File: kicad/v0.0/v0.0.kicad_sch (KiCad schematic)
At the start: 49 parts, among them J1 USB_B_Micro, J2 9V_IN, J3 LED, J4 MOTOR, Q1 IRF520, SW1 SW_Push, SW2 SW_Push, U1 MCP2221AxSL, U2 MAX14872ETC+, U3 ESP32-WROOM-32, U6 AZ1117-3.3

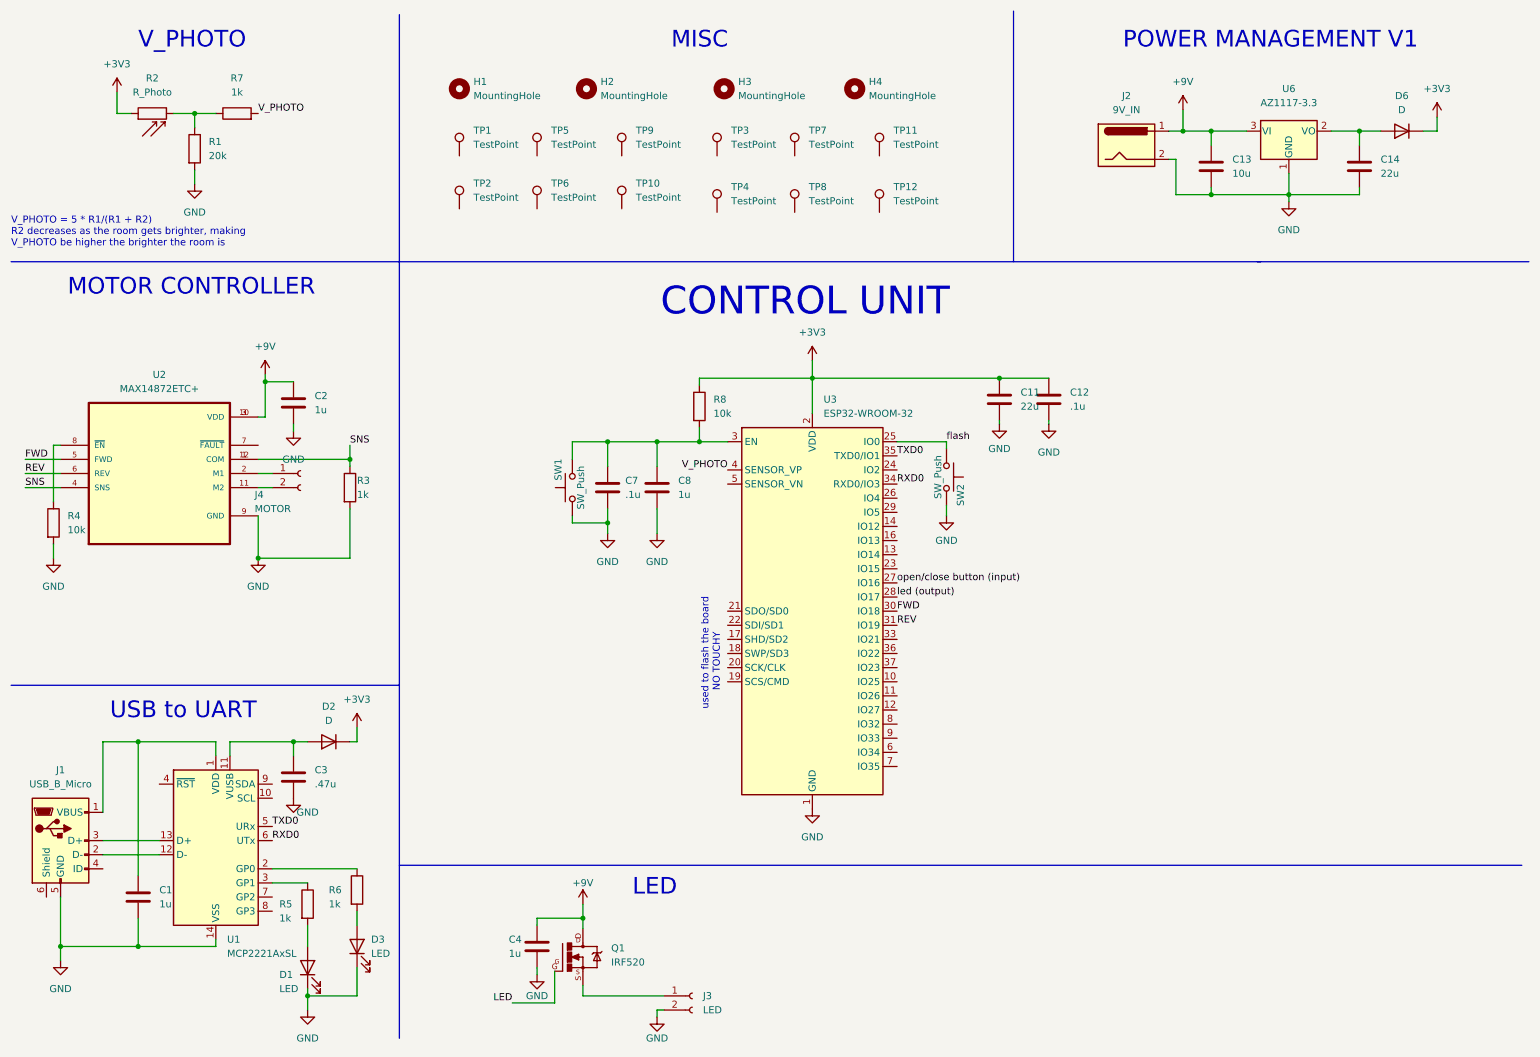
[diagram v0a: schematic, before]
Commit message: pcb is laid out, time to route
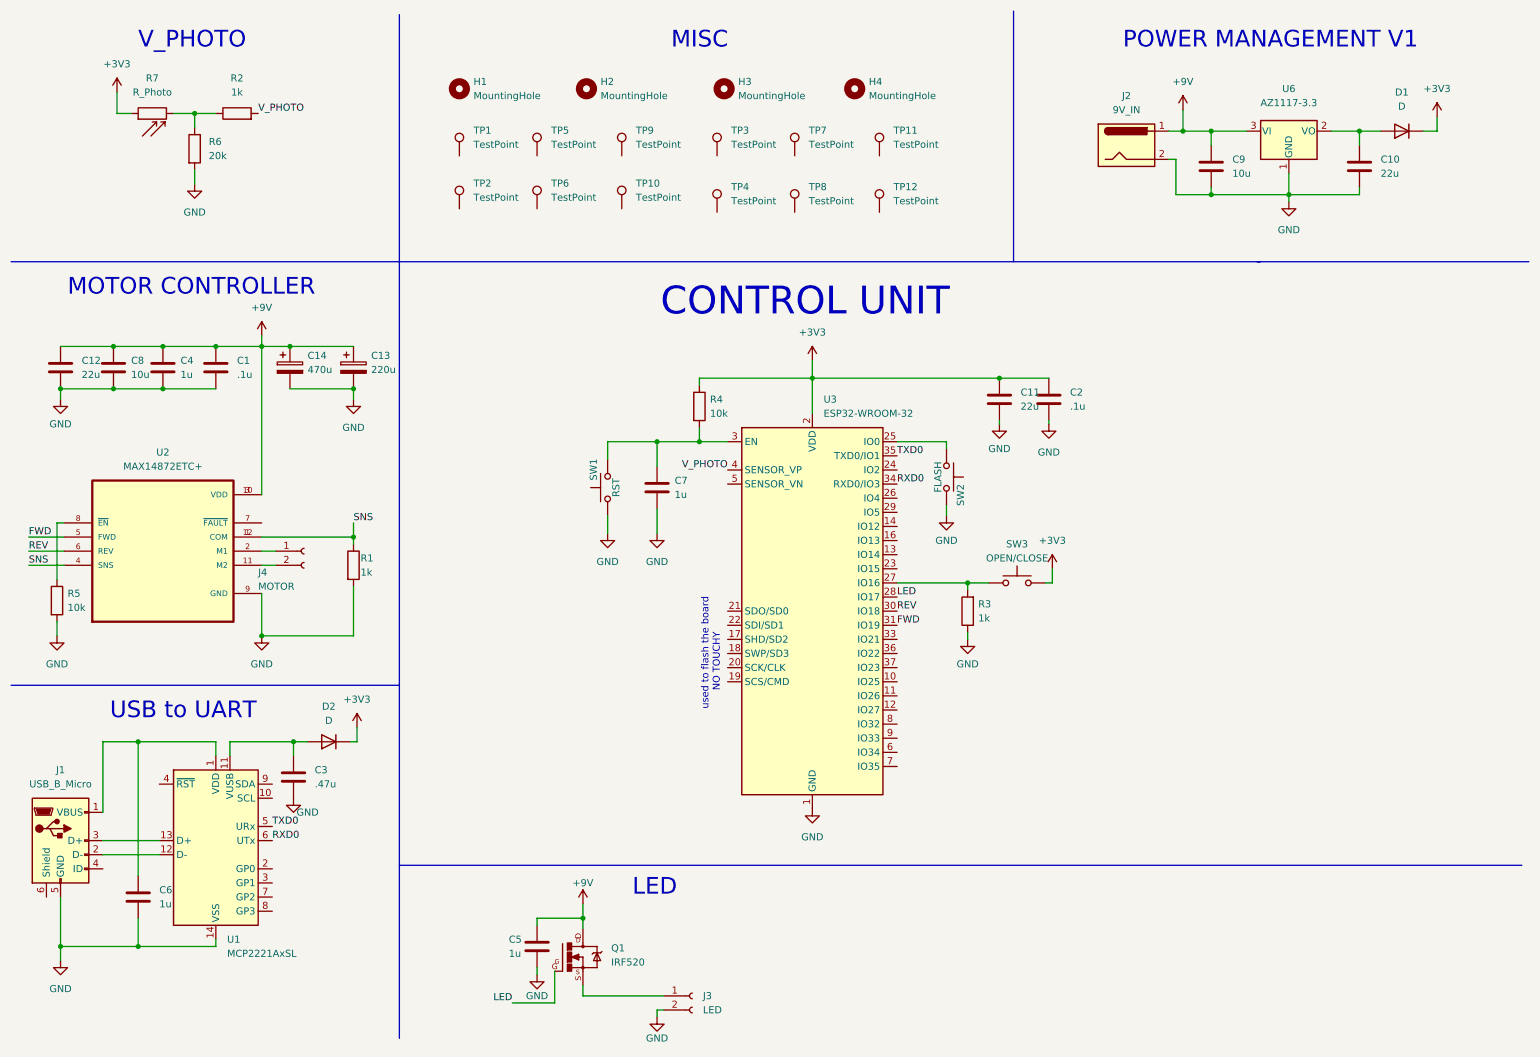
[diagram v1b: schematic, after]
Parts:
- removed C7: .1u, Capacitor_SMD:C_01005_0402Metric_Pad0.57x0.30mm_HandSolder, symbol Device:C
- removed D1, D3: LED, LED_SMD:LED_0603_1608Metric_Pad1.05x0.95mm_HandSolder, symbol Device:LED
- removed R5, R6: 1k, Resistor_SMD:R_0603_1608Metric_Pad0.98x0.95mm_HandSolder, symbol Device:R
- added C1: .1u, Capacitor_SMD:C_01005_0402Metric_Pad0.57x0.30mm_HandSolder, symbol Device:C
- added C13: 220u, Capacitor_THT:CP_Radial_D8.0mm_P3.50mm, symbol Device:C_Polarized
- added C14: 470u, Capacitor_THT:CP_Radial_D10.0mm_P5.00mm, symbol Device:C_Polarized
- added C4: 1u, Capacitor_SMD:C_0201_0603Metric_Pad0.64x0.40mm_HandSolder, symbol Device:C
- added C8: 10u, Capacitor_SMD:C_0805_2012Metric_Pad1.18x1.45mm_HandSolder, symbol Device:C
- added R3: 1k, Resistor_SMD:R_0603_1608Metric_Pad0.98x0.95mm_HandSolder, symbol Device:R
- added SW3: OPEN/CLOSE, Button_Switch_THT:SW_PUSH-12mm, symbol Switch:SW_Push
- C12: renamed from C2; value 1u -> 22u; footprint Capacitor_SMD:C_0201_0603Metric_Pad0.64x0.40mm_HandSolder -> Capacitor_SMD:C_1206_3216Metric_Pad1.33x1.80mm_HandSolder
- SW1: value SW_Push -> RST
- SW2: value SW_Push -> FLASH
- renumbered C14 to C10, C12 to C2, C4 to C5, C1 to C6, C8 to C7, C13 to C9, D6 to D1, R3 to R1, R7 to R2, R8 to R4, R4 to R5, R1 to R6, R2 to R7
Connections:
- net led (output) is gone; now on net LED: U3.28 (IO17)
- net +3V3: now also SW3.2
- net +9V: now also C1.1, C13.1, C14.1, C4.1, C8.1
- net FWD: now also U3.31 (IO19); no longer U3.30 (IO18)
- net GND: now also C1.2, C13.2, C14.2, C4.2, C8.2, R3.1
- net REV: now also U3.30 (IO18); no longer U3.31 (IO19)
- net flash: no longer names the net of SW2.1, U3.25 (IO0)
- net open/close button (input): no longer names the net of U3.27 (IO16)
- net open/close button (input): now also R3.2, SW3.1
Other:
- note removed: "V_PHOTO = 5 * R1/(R1 + R2) R2 decreases as the room gets brighter, making V_PHOTO be higher the brighter the room is"
- moved on the sheet: C12, J4, R1, R5, SW1, U2

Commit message: minor tweaks, im a lil bit of a control freak so i keep messing wit it
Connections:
- net GND: now also SW3.1
- net at R3.2, U3.27 (IO16): no longer SW3.1
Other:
- moved on the sheet: R3
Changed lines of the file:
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@@
   (junction (at 57.785 124.46) (diameter 0) (color 0 0 0 0)
   )
-  (junction (at 184.785 114.935) (diameter 0) (color 0 0 0 0)
-  )
   (junction (at 156.845 78.105) (diameter 0) (color 0 0 0 0)
   )
@@
   (junction (at 62.865 72.39) (diameter 0) (color 0 0 0 0)
   )
+  (junction (at 186.69 114.935) (diameter 0) (color 0 0 0 0)
+  )
   (wire (pts (xy 40.005 80.01) (xy 49.53 80.01))
     (stroke (width 0) (type default) (color 0 0 0 0))
@@
     (stroke (width 0) (type default) (color 0 0 0 0))
   )
-  (wire (pts (xy 172.085 114.935) (xy 184.785 114.935))
+  (wire (pts (xy 172.085 114.935) (xy 177.165 114.935))
     (stroke (width 0) (type default) (color 0 0 0 0))
   )
@@
     (stroke (width 0) (type default) (color 0 0 0 0))
   )
-  (wire (pts (xy 184.785 114.935) (xy 184.785 116.205))
+  (wire (pts (xy 186.69 114.935) (xy 186.69 125.095))
     (stroke (width 0) (type default) (color 0 0 0 0))
   )
@@
     (stroke (width 0) (type default) (color 0 0 0 0))
   )
+  (wire (pts (xy 186.69 114.935) (xy 188.595 114.935))
+    (stroke (width 0) (type default) (color 0 0 0 0))
+  )
   (wire (pts (xy 107.315 175.26) (xy 107.315 176.53))
     (stroke (width 0) (type default) (color 0 0 0 0))
@@
     (stroke (width 0) (type default) (color 0 0 0 0))
   )
-  (wire (pts (xy 184.785 114.935) (xy 188.595 114.935))
+  (wire (pts (xy 184.785 114.935) (xy 186.69 114.935))
     (stroke (width 0) (type default) (color 0 0 0 0))
   )
@@
   )
   (wire (pts (xy 223.52 29.845) (xy 223.52 33.655))
-    (stroke (width 0) (type default) (color 0 0 0 0))
-  )
-  (wire (pts (xy 184.785 123.825) (xy 184.785 125.095))
     (stroke (width 0) (type default) (color 0 0 0 0))
   )
@@
     (pin "3")
   )
-  (symbol (lib_id "power:GND") (at 184.785 125.095 0) (unit 1)
-    (in_bom yes) (on_board yes) (fields_autoplaced)
-    (property "Reference" "#PWR0102" (id 0) (at 184.785 131.445 0)
-      (effects (font (size 1.27 1.27)) hide)
-    )
-    (property "Value" "GND" (id 1) (at 184.785 129.54 0))
-    (property "Footprint" "" (id 2) (at 184.785 125.095 0)
-      (effects (font (size 1.27 1.27)) hide)
-    )
-    (property "Datasheet" "" (id 3) (at 184.785 125.095 0)
+  (symbol (lib_id "power:GND") (at 186.69 125.095 0) (unit 1)
+    (in_bom yes) (on_board yes) (fields_autoplaced)
+    (property "Reference" "#PWR0102" (id 0) (at 186.69 131.445 0)
+      (effects (font (size 1.27 1.27)) hide)
+    )
+    (property "Value" "GND" (id 1) (at 186.69 129.54 0))
+    (property "Footprint" "" (id 2) (at 186.69 125.095 0)
+      (effects (font (size 1.27 1.27)) hide)
+    )
+    (property "Datasheet" "" (id 3) (at 186.69 125.095 0)
       (effects (font (size 1.27 1.27)) hide)
     )
@@
     (pin "1")
   )
-  (symbol (lib_id "Device:R") (at 184.785 120.015 180) (unit 1)
-    (in_bom yes) (on_board yes) (fields_autoplaced)
-    (property "Reference" "R3" (id 0) (at 186.69 118.7449 0)
-      (effects (font (size 1.27 1.27)) (justify right))
-    )
-    (property "Value" "1k" (id 1) (at 186.69 121.2849 0)
-      (effects (font (size 1.27 1.27)) (justify right))
-    )
-    (property "Footprint" "Resistor_SMD:R_0603_1608Metric_Pad0.98x0.95mm_HandSolder" (id 2) (at 186.563 120.015 90)
-      (effects (font (size 1.27 1.27)) hide)
-    )
-    (property "Datasheet" "~" (id 3) (at 184.785 120.015 0)
-      (effects (font (size 1.27 1.27)) hide)
-    )
+  (symbol (lib_id "Device:R") (at 180.975 114.935 270) (unit 1)
+    (in_bom yes) (on_board yes) (fields_autoplaced)
+    (property "Reference" "R3" (id 0) (at 180.975 109.22 90))
+    (property "Value" "1k" (id 1) (at 180.975 111.76 90))
+    (property "Footprint" "Resistor_SMD:R_0603_1608Metric_Pad0.98x0.95mm_HandSolder" (id 2) (at 180.975 113.157 90)
+      (effects (font (size 1.27 1.27)) hide)
+    )
+    (property "Datasheet" "~" (id 3) (at 180.975 114.935 0)
+      (effects (font (size 1.27 1.27)) hide)
+    )

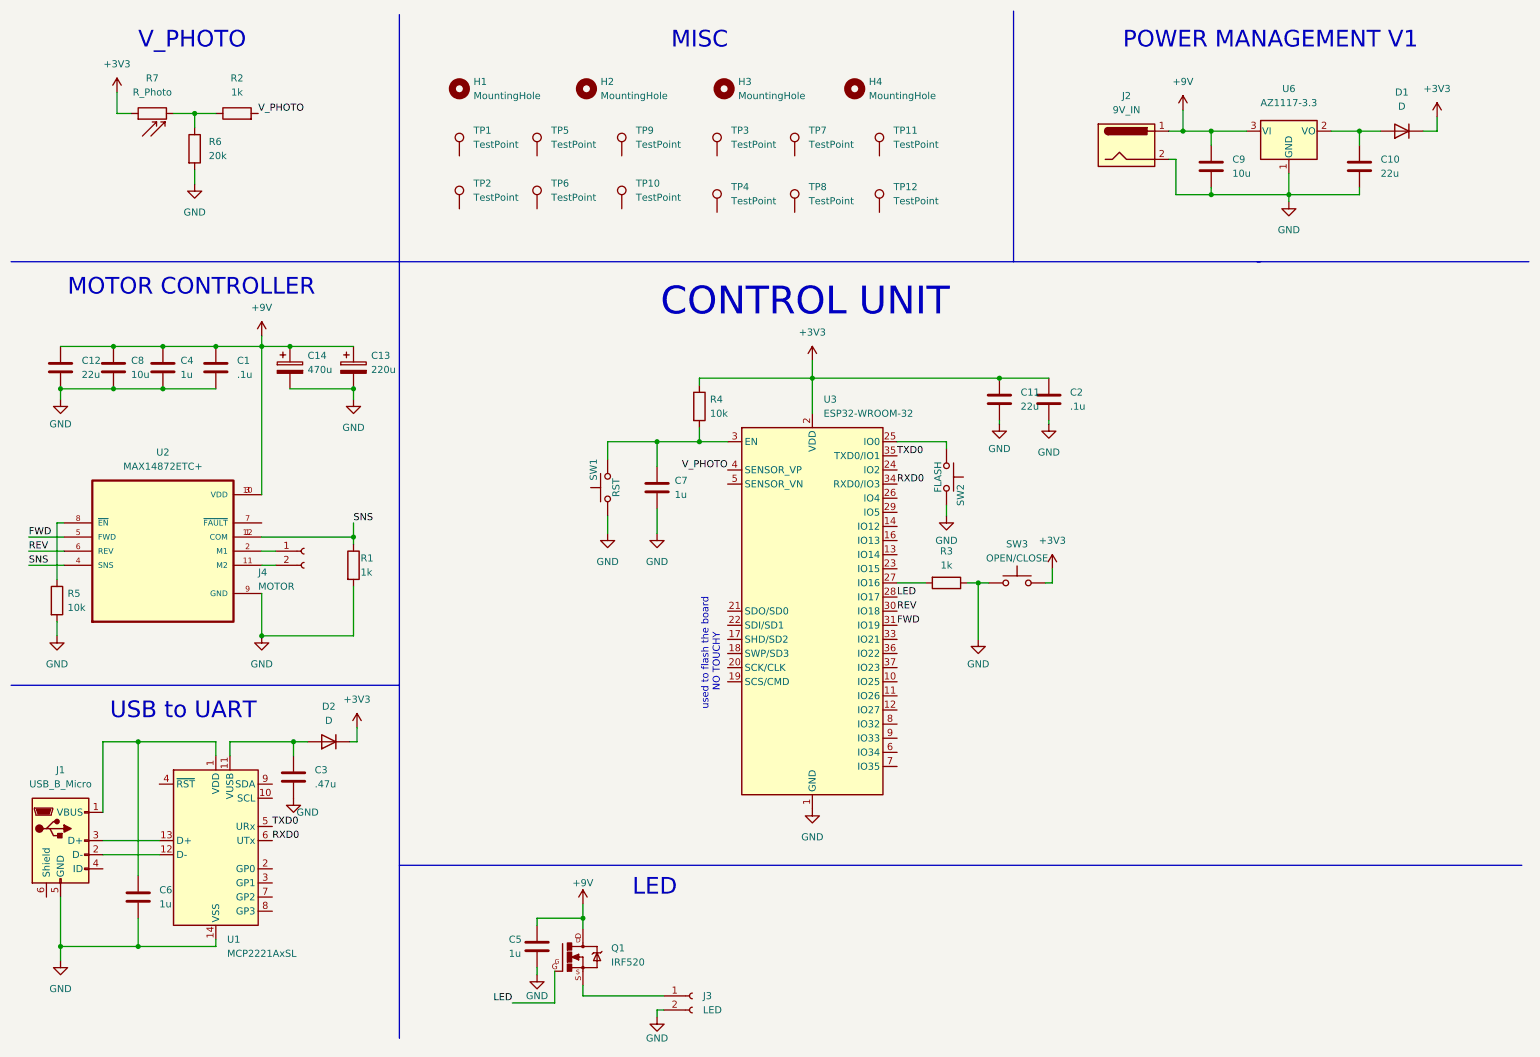
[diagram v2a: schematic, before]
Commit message: made resistors and capacitors standard size
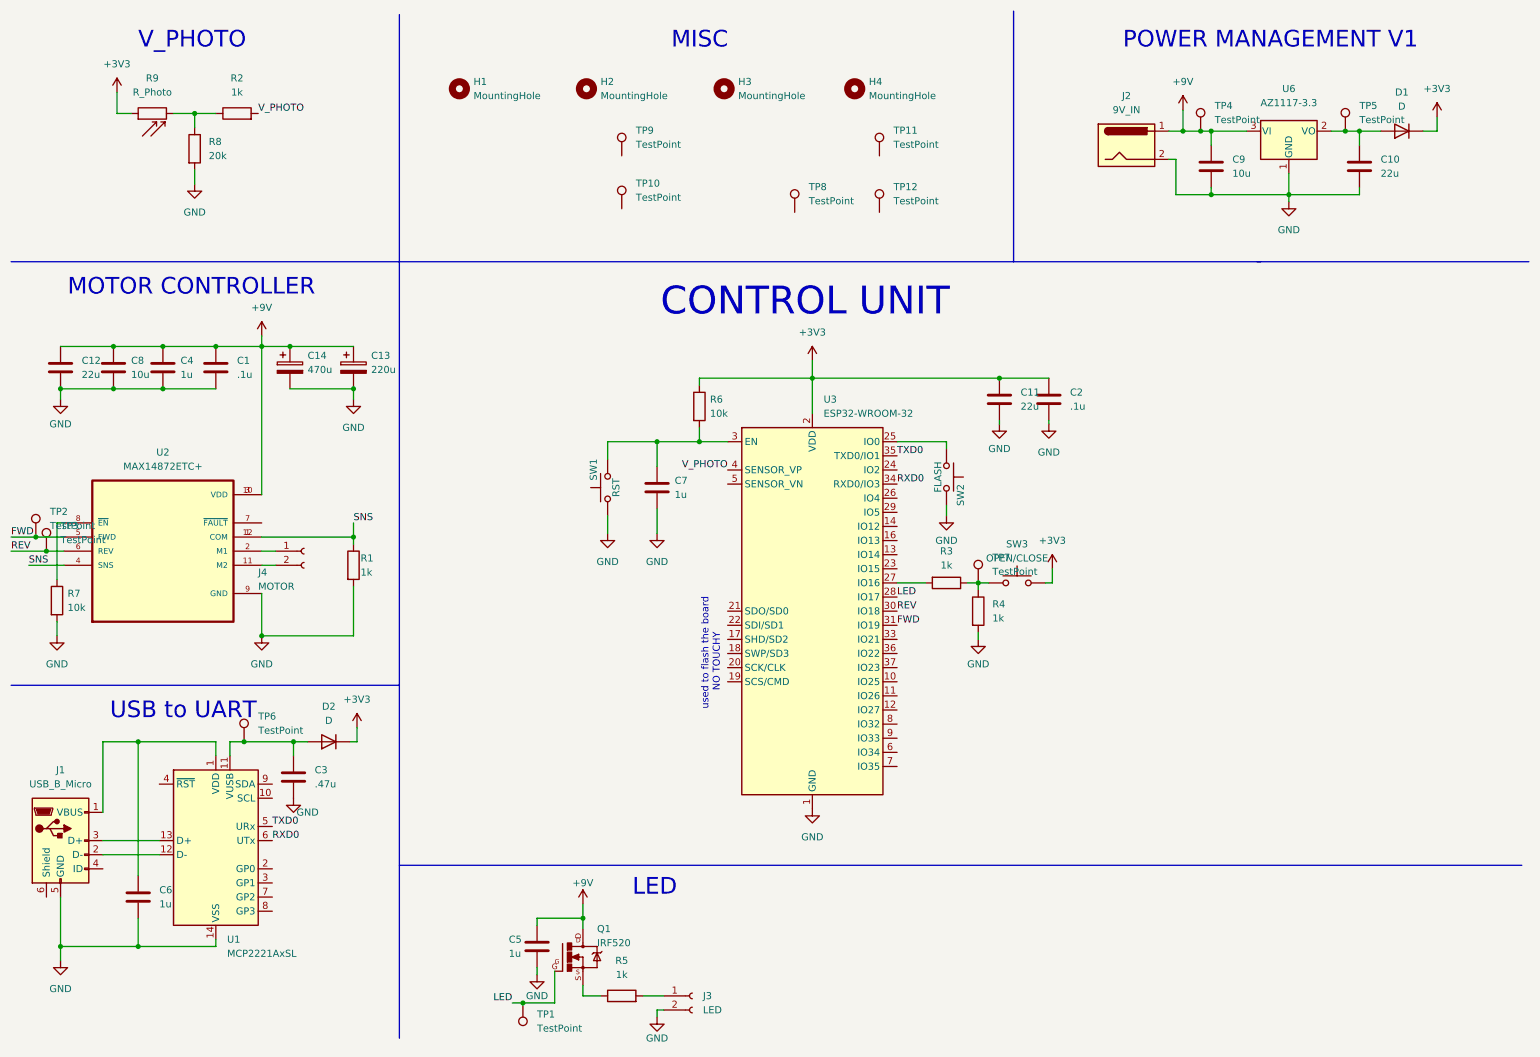
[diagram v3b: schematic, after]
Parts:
- added R4, R5: 1k, Resistor_SMD:R_0805_2012Metric_Pad1.20x1.40mm_HandSolder, symbol Device:R
- C1, C2: footprint Capacitor_SMD:C_01005_0402Metric_Pad0.57x0.30mm_HandSolder -> Capacitor_SMD:C_0805_2012Metric_Pad1.18x1.45mm_HandSolder
- C10, C11, C12: footprint Capacitor_SMD:C_1206_3216Metric_Pad1.33x1.80mm_HandSolder -> Capacitor_SMD:C_0805_2012Metric_Pad1.18x1.45mm_HandSolder
- C3: footprint Capacitor_SMD:C_0402_1005Metric_Pad0.74x0.62mm_HandSolder -> Capacitor_SMD:C_0805_2012Metric_Pad1.18x1.45mm_HandSolder
- C4, C5, C6, C7: footprint Capacitor_SMD:C_0201_0603Metric_Pad0.64x0.40mm_HandSolder -> Capacitor_SMD:C_0805_2012Metric_Pad1.18x1.45mm_HandSolder
- J2: footprint Connector_BarrelJack:BarrelJack_CUI_PJ-063AH_Horizontal -> Connector_BarrelJack:BarrelJack_CUI_PJ-102AH_Horizontal
- R1, R2, R3: footprint Resistor_SMD:R_0603_1608Metric_Pad0.98x0.95mm_HandSolder -> Resistor_SMD:R_0805_2012Metric_Pad1.20x1.40mm_HandSolder
- R6: renamed from R4; footprint Resistor_SMD:R_0201_0603Metric_Pad0.64x0.40mm_HandSolder -> Resistor_SMD:R_0805_2012Metric_Pad1.20x1.40mm_HandSolder
- R7: renamed from R5; footprint Resistor_SMD:R_0201_0603Metric_Pad0.64x0.40mm_HandSolder -> Resistor_SMD:R_0805_2012Metric_Pad1.20x1.40mm_HandSolder
- R8: renamed from R6; footprint Resistor_SMD:R_0603_1608Metric_Pad0.98x0.95mm_HandSolder -> Resistor_SMD:R_0805_2012Metric_Pad1.20x1.40mm_HandSolder
- renumbered R7 to R9
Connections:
- net +9V: now also TP4.1
- net FWD: now also TP2.1
- net GND: now also R4.2; no longer R3.1, SW3.1
- net LED: now also TP1.1
- net REV: now also TP3.1
- net at C10.1, D1.2 (A), U6.2 (VO): now also TP5.1
- net at C3.1, D2.2 (A), U1.11 (VUSB): now also TP6.1
- net at J3.1 (Pin_1): now also R5.2; no longer Q1.S
- net at TP7.1: now also R3.1, SW3.1, R4.1
- new net: Q1.S, R5.1
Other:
- moved on the sheet: TP1, TP2, TP3, TP4, TP5, TP6, TP7
